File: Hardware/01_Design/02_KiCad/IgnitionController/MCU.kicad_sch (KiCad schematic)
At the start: 0 parts

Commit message: MCU sheet Initial commit
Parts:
- added C16, C17, C18, C19: 12p, symbol Device:C_Small
- added C20, C22, C24, C26, C28, C30, C32, C34, C36: 0.1u, symbol Device:C_Small
- added C21, C23, C25, C27, C29, C31, C33, C35: 1u, symbol Device:C_Small
- added D1, D2, D3, D4, D5: RED, symbol Device:LED
- added R1, R4: 10k, symbol Device:R_Small
- added R2: 510R, symbol Device:R_Small
- added R3: 0R, symbol Device:R_Small
- added R40, R41, R42, R43, R44: 470R, symbol Device:R_Small
- added TP10: Cyl1_TP, symbol Connector:TestPoint
- added TP11: Cyl2_TP, symbol Connector:TestPoint
- added TP12: Sig1_TP, symbol Connector:TestPoint
- added TP13: Sig2_TP, symbol Connector:TestPoint
- added U12: STM32F407VGTx, Package_QFP:LQFP-100_14x14mm_P0.5mm, symbol Library_sym.pretty:STM32F407VGTx
- added Y2: 32.768kHz, symbol Device:Crystal_Small
- added Y3: 8MHz, symbol Device:Crystal_Small
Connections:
- new net: C18.2, U12.12 (PH0), Y3.2
- new net: C17.1, U12.8 (PC14), Y2.1
- new net: C16.2, U12.9 (PC15), Y2.2
- new net: R44.1, U12.62 (PD15)
- new net: D5.2 (A), R44.2
- new net: D2.2 (A), R41.2
- new net: D4.2 (A), R43.2
- new net: C19.1, U12.13 (PH1), Y3.1
- new net: C20.1, R4.2, U12.14 (NRST)
- new net: R1.2, R2.1, U12.94 (BOOT0)
- new net: D3.2 (A), R42.2
- new net: D1.2 (A), R40.2
- new net: R2.2, R3.1
- new net CAN_RXD: U12.95 (PB8)
- new net CAN_TXD: U12.96 (PB9)
- new net Cylinder1Out_Pin: R41.1, TP10.1, U12.53 (PB14)
- new net Cylinder2Out_Pin: R40.1, TP11.1, U12.52 (PB13)
- new net GND: C16.1, C17.2, C18.1, C19.2, C20.2, C21.2, C22.2, C23.2, C24.2, C25.2, C26.2, C27.2, C28.2, C29.2, C30.2, C31.2, C32.2, C33.2, C34.2, C35.2, C36.2, D1.1 (K), D2.1 (K), D3.1 (K), D4.1 (K), D5.1 (K), R3.2, U12.10 (VSS), U12.20 (VSSA), U12.27 (VSS), U12.74 (VSS), U12.99 (VSS)
- new net I2C_SCL: U12.92 (PB6)
- new net I2C_SDA: U12.93 (PB7)
- new net MCU_SPI_CS: U12.67 (PA8)
- new net MCU_SPI_MISO: U12.31 (PA6)
- new net MCU_SPI_MOSI: U12.32 (PA7)
- new net MCU_SPI_SCK: U12.30 (PA5)
- new net OE_PIN: U12.68 (PA9)
- new net SWCLK_Pin: U12.76 (PA14)
- new net SWDIO_Pin: U12.72 (PA13)
- new net Signal1_Pin: R42.1, TP12.1, U12.29 (PA4)
- new net Signal2_Pin: TP13.1, U12.41 (PE10)
- new net UART_RX: U12.79 (PC11)
- new net UART_TX: U12.78 (PC10)
- new net VMCU: C21.1, C22.1, C23.1, C24.1, C25.1, C26.1, C27.1, C28.1, C29.1, C30.1, C31.1, C32.1, C33.1, C34.1, C35.1, C36.1, R1.1, R4.1, U12.100 (VDD), U12.11 (VDD), U12.19 (VDD), U12.21 (VREF+), U12.22 (VDDA), U12.28 (VDD), U12.50 (VDD), U12.75 (VDD)

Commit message: Peripherals Update
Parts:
- removed D1, D2: RED, symbol Device:LED
- removed R40, R41: 470R, symbol Device:R_Small
- added TP14: Cyl3_TP, symbol Connector:TestPoint
- added TP15: Cyl4_TP, symbol Connector:TestPoint
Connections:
- net ADC_VMCU: now reaches U12.24 (PA1)
- net ADC_VSENS: now reaches U12.25 (PA2)
- net ADC_VBAT: now reaches U12.26 (PA3)
- net ADC_VIGNTION: now reaches U12.35 (PB0)
- net Cylinder4Out_Pin: now reaches U12.48 (PB11)
- net Cylinder4Out_Pin: now also TP15.1
- net Cylinder3Out_Pin: now reaches U12.51 (PB12)
- net Cylinder3Out_Pin: now also TP14.1
- net OE_PIN2: now reaches U12.69 (PA10)
- net VMCU renamed VMCU_OUT

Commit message: Updates to HW Layout
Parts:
- C16, C17, C18, C19, C20, C21, C22, C23, C24, C25, C26, C27, C28, C29, C30, C31, C32, C33, C34, C35, C36: footprint (none) -> Capacitor_SMD:C_0805_2012Metric_Pad1.18x1.45mm_HandSolder
- D3, D4, D5: footprint (none) -> LED_SMD:LED_1206_3216Metric_Pad1.42x1.75mm_HandSolder
- R1, R2, R3, R4, R42, R43, R44: footprint (none) -> Resistor_SMD:R_0805_2012Metric_Pad1.20x1.40mm_HandSolder
- TP10, TP11, TP12, TP13, TP14, TP15: footprint (none) -> TestPoint:TestPoint_Pad_1.0x1.0mm
- Y2, Y3: footprint (none) -> Crystal:Crystal_HC52-8mm_Horizontal
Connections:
- net Signal2_Pin: now also R43.1
- net MCU_NRST: now reaches C20.1, R4.2, U12.14 (NRST)
- net TPS_ADC_SIGNAL: now reaches U12.15 (PC0)
- net MAP_SENSOR_ADC_SIGNAL: now reaches U12.16 (PC1)
- net COOLANT_TEMP_ADC_SIGNAL: now reaches U12.17 (PC2)
- net Cylinder1FuelOut_Pin: now reaches U12.63 (PC6)
- net Cylinder2FuelOut_Pin: now reaches U12.64 (PC7)
- net Cylinder3FuelOut_Pin: now reaches U12.65 (PC8)
- net Cylinder4FuelOut_Pin: now reaches U12.66 (PC9)
- no-connect marks 0 -> 49
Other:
- moved on the sheet: D4, R43

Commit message: Initial routing of Power supply
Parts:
- C16, C17, C18, C19, C20, C21, C22, C23, C24, C25, C26, C27, C28, C29, C30, C31, C32, C33, C34, C35, C36: footprint Capacitor_SMD:C_0805_2012Metric_Pad1.18x1.45mm_HandSolder -> Capacitor_SMD:C_0603_1608Metric_Pad1.08x0.95mm_HandSolder
- R1, R2, R3, R4, R42, R43, R44: footprint Resistor_SMD:R_0805_2012Metric_Pad1.20x1.40mm_HandSolder -> Resistor_SMD:R_0603_1608Metric_Pad0.98x0.95mm_HandSolder
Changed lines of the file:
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@@
 			)
 		)
-		(property "Footprint" "Capacitor_SMD:C_0805_2012Metric_Pad1.18x1.45mm_HandSolder"
+		(property "Footprint" "Capacitor_SMD:C_0603_1608Metric_Pad1.08x0.95mm_HandSolder"
 			(at 53.34 187.96 0)
 			(effects
@@
 			)
 		)
-		(property "Footprint" "Capacitor_SMD:C_0805_2012Metric_Pad1.18x1.45mm_HandSolder"
+		(property "Footprint" "Capacitor_SMD:C_0603_1608Metric_Pad1.08x0.95mm_HandSolder"
 			(at 189.23 133.35 0)
 			(effects
@@
 			)
 		)
-		(property "Footprint" "Capacitor_SMD:C_0805_2012Metric_Pad1.18x1.45mm_HandSolder"
+		(property "Footprint" "Capacitor_SMD:C_0603_1608Metric_Pad1.08x0.95mm_HandSolder"
 			(at 90.17 187.96 0)
 			(effects
@@
 			)
 		)
-		(property "Footprint" "Resistor_SMD:R_0805_2012Metric_Pad1.20x1.40mm_HandSolder"
+		(property "Footprint" "Resistor_SMD:R_0603_1608Metric_Pad0.98x0.95mm_HandSolder"
 			(at 194.31 55.88 0)
 			(effects
@@
 			)
 		)
-		(property "Footprint" "Capacitor_SMD:C_0805_2012Metric_Pad1.18x1.45mm_HandSolder"
+		(property "Footprint" "Capacitor_SMD:C_0603_1608Metric_Pad1.08x0.95mm_HandSolder"
 			(at 45.72 187.96 0)
 			(effects
@@
 			)
 		)
-		(property "Footprint" "Capacitor_SMD:C_0805_2012Metric_Pad1.18x1.45mm_HandSolder"
+		(property "Footprint" "Capacitor_SMD:C_0603_1608Metric_Pad1.08x0.95mm_HandSolder"
 			(at 72.39 187.96 0)
 			(effects
@@
 			)
 		)
-		(property "Footprint" "Capacitor_SMD:C_0805_2012Metric_Pad1.18x1.45mm_HandSolder"
+		(property "Footprint" "Capacitor_SMD:C_0603_1608Metric_Pad1.08x0.95mm_HandSolder"
 			(at 189.23 128.27 0)
 			(effects
@@
 			)
 		)
-		(property "Footprint" "Capacitor_SMD:C_0805_2012Metric_Pad1.18x1.45mm_HandSolder"
+		(property "Footprint" "Capacitor_SMD:C_0603_1608Metric_Pad1.08x0.95mm_HandSolder"
 			(at 82.55 187.96 0)
 			(effects
@@
 			)
 		)
-		(property "Footprint" "Resistor_SMD:R_0805_2012Metric_Pad1.20x1.40mm_HandSolder"
+		(property "Footprint" "Resistor_SMD:R_0603_1608Metric_Pad0.98x0.95mm_HandSolder"
 			(at 52.07 144.78 0)
 			(effects
@@
 			)
 		)
-		(property "Footprint" "Capacitor_SMD:C_0805_2012Metric_Pad1.18x1.45mm_HandSolder"
+		(property "Footprint" "Capacitor_SMD:C_0603_1608Metric_Pad1.08x0.95mm_HandSolder"
 			(at 33.02 186.69 0)
 			(effects
@@
 			)
 		)
-		(property "Footprint" "Capacitor_SMD:C_0805_2012Metric_Pad1.18x1.45mm_HandSolder"
+		(property "Footprint" "Capacitor_SMD:C_0603_1608Metric_Pad1.08x0.95mm_HandSolder"
 			(at 99.06 187.96 0)
 			(effects
@@
 			)
 		)
-		(property "Footprint" "Capacitor_SMD:C_0805_2012Metric_Pad1.18x1.45mm_HandSolder"
+		(property "Footprint" "Capacitor_SMD:C_0603_1608Metric_Pad1.08x0.95mm_HandSolder"
 			(at 123.19 189.23 0)
 			(effects
@@
 			)
 		)
-		(property "Footprint" "Resistor_SMD:R_0805_2012Metric_Pad1.20x1.40mm_HandSolder"
+		(property "Footprint" "Resistor_SMD:R_0603_1608Metric_Pad0.98x0.95mm_HandSolder"
 			(at 210.82 142.24 0)
 			(effects
@@
 			)
 		)
-		(property "Footprint" "Capacitor_SMD:C_0805_2012Metric_Pad1.18x1.45mm_HandSolder"
+		(property "Footprint" "Capacitor_SMD:C_0603_1608Metric_Pad1.08x0.95mm_HandSolder"
 			(at 26.67 168.91 0)
 			(effects
@@
 			)
 		)
-		(property "Footprint" "Resistor_SMD:R_0805_2012Metric_Pad1.20x1.40mm_HandSolder"
+		(property "Footprint" "Resistor_SMD:R_0603_1608Metric_Pad0.98x0.95mm_HandSolder"
 			(at 217.17 100.33 0)
 			(effects
@@
 			)
 		)
-		(property "Footprint" "Capacitor_SMD:C_0805_2012Metric_Pad1.18x1.45mm_HandSolder"
+		(property "Footprint" "Capacitor_SMD:C_0603_1608Metric_Pad1.08x0.95mm_HandSolder"
 			(at 106.68 187.96 0)
 			(effects
@@
 			)
 		)
-		(property "Footprint" "Capacitor_SMD:C_0805_2012Metric_Pad1.18x1.45mm_HandSolder"
+		(property "Footprint" "Capacitor_SMD:C_0603_1608Metric_Pad1.08x0.95mm_HandSolder"
 			(at 34.29 168.91 0)
 			(effects
@@
 			)
 		)
-		(property "Footprint" "Capacitor_SMD:C_0805_2012Metric_Pad1.18x1.45mm_HandSolder"
+		(property "Footprint" "Capacitor_SMD:C_0603_1608Metric_Pad1.08x0.95mm_HandSolder"
 			(at 115.57 189.23 0)
 			(effects
@@
 			)
 		)
-		(property "Footprint" "Capacitor_SMD:C_0805_2012Metric_Pad1.18x1.45mm_HandSolder"
+		(property "Footprint" "Capacitor_SMD:C_0603_1608Metric_Pad1.08x0.95mm_HandSolder"
 			(at 64.77 187.96 0)
 			(effects
@@
 			)
 		)
-		(property "Footprint" "Resistor_SMD:R_0805_2012Metric_Pad1.20x1.40mm_HandSolder"
+		(property "Footprint" "Resistor_SMD:R_0603_1608Metric_Pad0.98x0.95mm_HandSolder"
 			(at 219.71 143.51 0)
 			(effects
@@
 			)
 		)
-		(property "Footprint" "Capacitor_SMD:C_0805_2012Metric_Pad1.18x1.45mm_HandSolder"
+		(property "Footprint" "Capacitor_SMD:C_0603_1608Metric_Pad1.08x0.95mm_HandSolder"
 			(at 180.34 148.59 0)
 			(effects
@@
 			)
 		)
-		(property "Footprint" "Capacitor_SMD:C_0805_2012Metric_Pad1.18x1.45mm_HandSolder"
+		(property "Footprint" "Capacitor_SMD:C_0603_1608Metric_Pad1.08x0.95mm_HandSolder"
 			(at 210.82 154.94 0)
 			(effects
@@
 			)
 		)
-		(property "Footprint" "Capacitor_SMD:C_0805_2012Metric_Pad1.18x1.45mm_HandSolder"
+		(property "Footprint" "Capacitor_SMD:C_0603_1608Metric_Pad1.08x0.95mm_HandSolder"
 			(at 82.55 38.1 0)
 			(effects
@@
 			)
 		)
-		(property "Footprint" "Capacitor_SMD:C_0805_2012Metric_Pad1.18x1.45mm_HandSolder"
+		(property "Footprint" "Capacitor_SMD:C_0603_1608Metric_Pad1.08x0.95mm_HandSolder"
 			(at 82.55 33.02 0)
 			(effects
@@
 			)
 		)
-		(property "Footprint" "Resistor_SMD:R_0805_2012Metric_Pad1.20x1.40mm_HandSolder"
+		(property "Footprint" "Resistor_SMD:R_0603_1608Metric_Pad0.98x0.95mm_HandSolder"
 			(at 231.14 148.59 0)
 			(effects
@@
 			)
 		)
-		(property "Footprint" "Capacitor_SMD:C_0805_2012Metric_Pad1.18x1.45mm_HandSolder"
+		(property "Footprint" "Capacitor_SMD:C_0603_1608Metric_Pad1.08x0.95mm_HandSolder"
 			(at 25.4 186.69 0)
 			(effects
@@
 			)
 		)
-		(property "Footprint" "Resistor_SMD:R_0805_2012Metric_Pad1.20x1.40mm_HandSolder"
+		(property "Footprint" "Resistor_SMD:R_0603_1608Metric_Pad0.98x0.95mm_HandSolder"
 			(at 238.76 152.4 0)
 			(effects
@@
 			)
 		)
-		(property "Footprint" "Capacitor_SMD:C_0805_2012Metric_Pad1.18x1.45mm_HandSolder"
+		(property "Footprint" "Capacitor_SMD:C_0603_1608Metric_Pad1.08x0.95mm_HandSolder"
 			(at 187.96 148.59 0)
 			(effects

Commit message: MCU HW Initial Layout
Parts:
- removed Y2: 32.768kHz, Crystal:Crystal_HC52-8mm_Horizontal, symbol Device:Crystal_Small
- removed Y3: 8MHz, Crystal:Crystal_HC52-8mm_Horizontal, symbol Device:Crystal_Small
- added Y1: FL0800011Q, FL0800011Q, symbol FL0800011Q:FL0800011Q
- added Y3: XT1312HHRXX32K76E, XT1312HHRXX32K76E, symbol XT1312HHRXX32K76E:XT1312HHRXX32K76E
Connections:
- net GND: now also C18.2, Y1.2 (GND_1), Y1.4 (GND_2); no longer C18.1
- net at U12.12 (PH0): now also C18.1, Y1.1 (CRYSTAL_1); no longer C18.2
- net at C17.1, U12.8 (PC14): now also Y3.1
- net at C16.2, U12.9 (PC15): now also Y3.2
- net at C19.1, U12.13 (PH1): now also Y1.3 (CRYSTAL_2)
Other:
- moved on the sheet: C18, C19

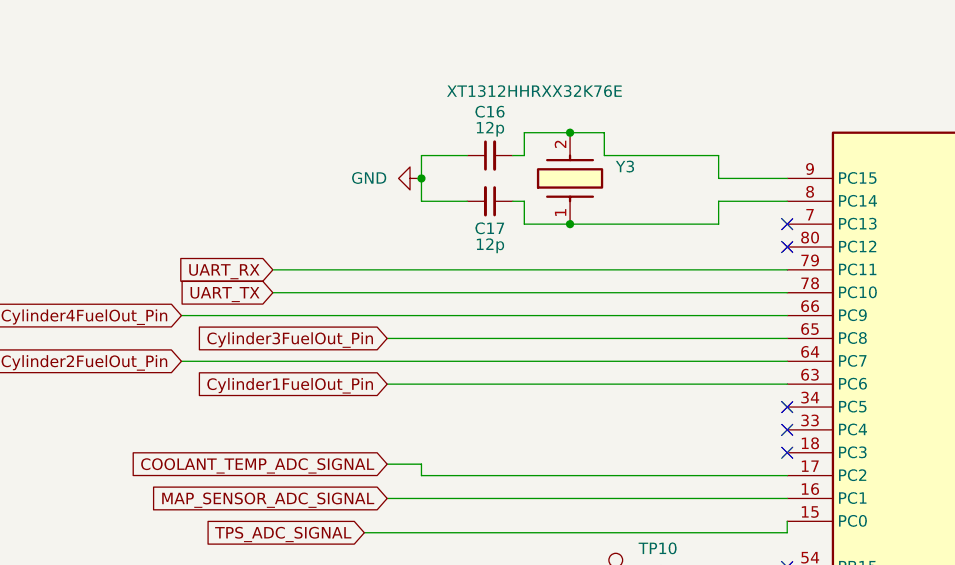
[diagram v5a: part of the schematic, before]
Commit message: Updated Solder Mask labels
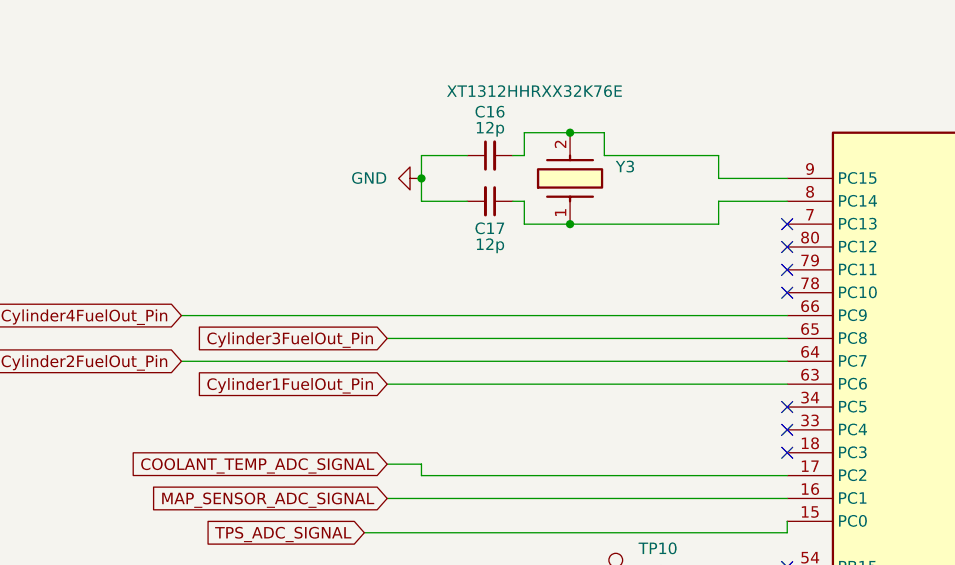
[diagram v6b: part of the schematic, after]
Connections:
- net UART_RX: no longer names the net of U12.79 (PC11)
- net UART_TX: no longer names the net of U12.78 (PC10)
- no-connect marks 49 -> 51
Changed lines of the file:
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@@
+	)
+	(no_connect
+		(at 115.57 45.72)
 	)
 	(no_connect
@@
 	)
 	(no_connect
+		(at 115.57 48.26)
+	)
+	(no_connect
 		(at 166.37 48.26)
 	)
@@
 	(wire
 		(pts
-			(xy 58.42 48.26) (xy 115.57 48.26)
-		)
-		(stroke
-			(width 0)
-			(type default)
-		)
-	)
-	(wire
-		(pts
 			(xy 114.3 134.62) (xy 115.57 134.62)
 		)
@@
 	(wire
 		(pts
-			(xy 58.42 45.72) (xy 115.57 45.72)
-		)
-		(stroke
-			(width 0)
-			(type default)
-		)
-	)
-	(wire
-		(pts
 			(xy 186.69 123.19) (xy 181.61 123.19)
 		)
@@
 		)
 	)
-	(global_label "UART_TX"
-		(shape input)
-		(at 58.42 48.26 180)
+	(global_label "MCU_SPI_SCK"
+		(shape input)
+		(at 40.64 137.16 180)
 		(fields_autoplaced yes)
 		(effects
@@
 		)
 		(property "Intersheetrefs" "${INTERSHEET_REFS}"
-			(at 47.6334 48.26 0)
+			(at 24.8339 137.16 0)
 			(effects
 				(font
@@
 		)
 	)
-	(global_label "MCU_SPI_SCK"
-		(shape input)
-		(at 40.64 137.16 180)
+	(global_label "ADC_VIGNTION"
+		(shape input)
+		(at 41.91 105.41 180)
 		(fields_autoplaced yes)
 		(effects
@@
 		)
 		(property "Intersheetrefs" "${INTERSHEET_REFS}"
-			(at 24.8339 137.16 0)
+			(at 25.8013 105.41 0)
 			(effects
 				(font
@@
 		)
 	)
-	(global_label "ADC_VIGNTION"
-		(shape input)
-		(at 41.91 105.41 180)
+	(global_label "Cylinder4Out_Pin"
+		(shape input)
+		(at 43.18 90.17 180)
 		(fields_autoplaced yes)
 		(effects
@@
 		)
 		(property "Intersheetrefs" "${INTERSHEET_REFS}"
-			(at 25.8013 105.41 0)
+			(at 24.1083 90.17 0)
 			(effects
 				(font
@@
 		)
 	)
-	(global_label "Cylinder4Out_Pin"
-		(shape input)
-		(at 43.18 90.17 180)
+	(global_label "ADC_VMCU"
+		(shape input)
+		(at 54.61 171.45 180)
 		(fields_autoplaced yes)
 		(effects
@@
 		)
 		(property "Intersheetrefs" "${INTERSHEET_REFS}"
-			(at 24.1083 90.17 0)
+			(at 41.8881 171.45 0)
 			(effects
 				(font
@@
 		)
 	)
-	(global_label "ADC_VMCU"
-		(shape input)
-		(at 54.61 171.45 180)
+	(global_label "MCU_SPI_MISO"
+		(shape input)
+		(at 40.64 133.35 180)
 		(fields_autoplaced yes)
 		(effects
@@
 		)
 		(property "Intersheetrefs" "${INTERSHEET_REFS}"
-			(at 41.8881 171.45 0)
+			(at 23.9872 133.35 0)
 			(effects
 				(font
@@
 		)
 	)
-	(global_label "MCU_SPI_MISO"
-		(shape input)
-		(at 40.64 133.35 180)
+	(global_label "Signal2_Pin"
+		(shape input)
+		(at 186.69 111.76 0)
+		(fields_autoplaced yes)
+		(effects
+			(font
+				(size 1.27 1.27)
+			)
+			(justify left)
+		)
+		(property "Intersheetrefs" "${INTERSHEET_REFS}"
+			(at 200.8026 111.76 0)
+			(effects
+				(font
+					(size 1.27 1.27)
+				)
+				(justify left)
+				(hide yes)
+			)
+		)
+	)
+	(global_label "CAN_TXD"
+		(shape input)
+		(at 80.01 93.98 180)
 		(fields_autoplaced yes)
 		(effects
@@
 		)
 		(property "Intersheetrefs" "${INTERSHEET_REFS}"
-			(at 23.9872 133.35 0)
+			(at 68.921 93.98 0)
 			(effects
 				(font
@@
 		)
 	)
-	(global_label "Signal2_Pin"
-		(shape input)
-		(at 186.69 111.76 0)
-		(fields_autoplaced yes)
-		(effects
-			(font
-				(size 1.27 1.27)
-			)
-			(justify left)
-		)
-		(property "Intersheetrefs" "${INTERSHEET_REFS}"
-			(at 200.8026 111.76 0)
-			(effects
-				(font
-					(size 1.27 1.27)
-				)
-				(justify left)
-				(hide yes)
-			)
-		)
-	)
-	(global_label "CAN_TXD"
-		(shape input)
-		(at 80.01 93.98 180)
+	(global_label "SWCLK_Pin"
+		(shape input)
+		(at 39.37 114.3 180)
 		(fields_autoplaced yes)
 		(effects
@@
 		)
 		(property "Intersheetrefs" "${INTERSHEET_REFS}"
-			(at 68.921 93.98 0)
+			(at 25.9829 114.3 0)
 			(effects
 				(font
@@
 		)
 	)
-	(global_label "SWCLK_Pin"
-		(shape input)
-		(at 39.37 114.3 180)
+	(global_label "Cylinder2FuelOut_Pin"
+		(shape input)
+		(at 48.26 55.88 180)
 		(fields_autoplaced yes)
 		(effects
@@
 		)
 		(property "Intersheetrefs" "${INTERSHEET_REFS}"
-			(at 25.9829 114.3 0)
-			(effects
-				(font
-					(size 1.27 1.27)
-				)
-				(justify right)
-				(hide yes)
-			)
-		)
-	)
-	(global_label "Cylinder2FuelOut_Pin"
-		(shape input)
-		(at 48.26 55.88 180)
-		(fields_autoplaced yes)
-		(effects
-			(font
-				(size 1.27 1.27)
-			)
-			(justify right)
-		)
-		(property "Intersheetrefs" "${INTERSHEET_REFS}"
 			(at 25.1969 55.88 0)
 			(effects
 				(font
-					(size 1.27 1.27)
-				)
-				(justify right)
-				(hide yes)
-			)
-		)
-	)
-	(global_label "UART_RX"
-		(shape input)
-		(at 58.42 45.72 180)
-		(fields_autoplaced yes)
-		(effects
-			(font
-				(size 1.27 1.27)
-			)
-			(justify right)
-		)
-		(property "Intersheetrefs" "${INTERSHEET_REFS}"
-			(at 47.331 45.72 0)
-			(effects
-				(font
